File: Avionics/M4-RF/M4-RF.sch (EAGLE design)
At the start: 25 parts, among them J1 132134RP, U1 CC1120, U2 CC1190, U3 CC2520, U4 CC2592, U5 INF-PG-LQFP-100-11-7000X7000E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

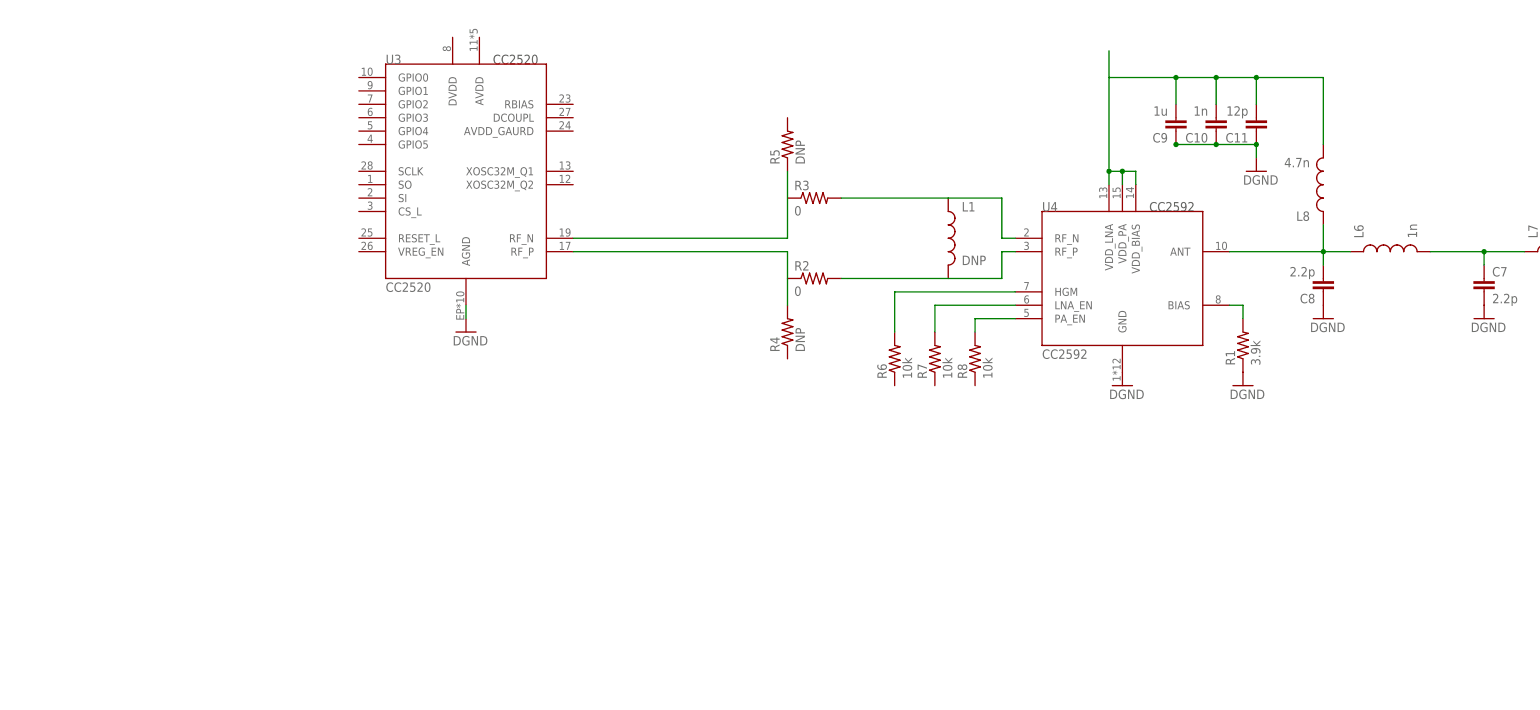
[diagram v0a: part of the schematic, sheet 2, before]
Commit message: Fixed library references and added balun to 2.4GHz circuit
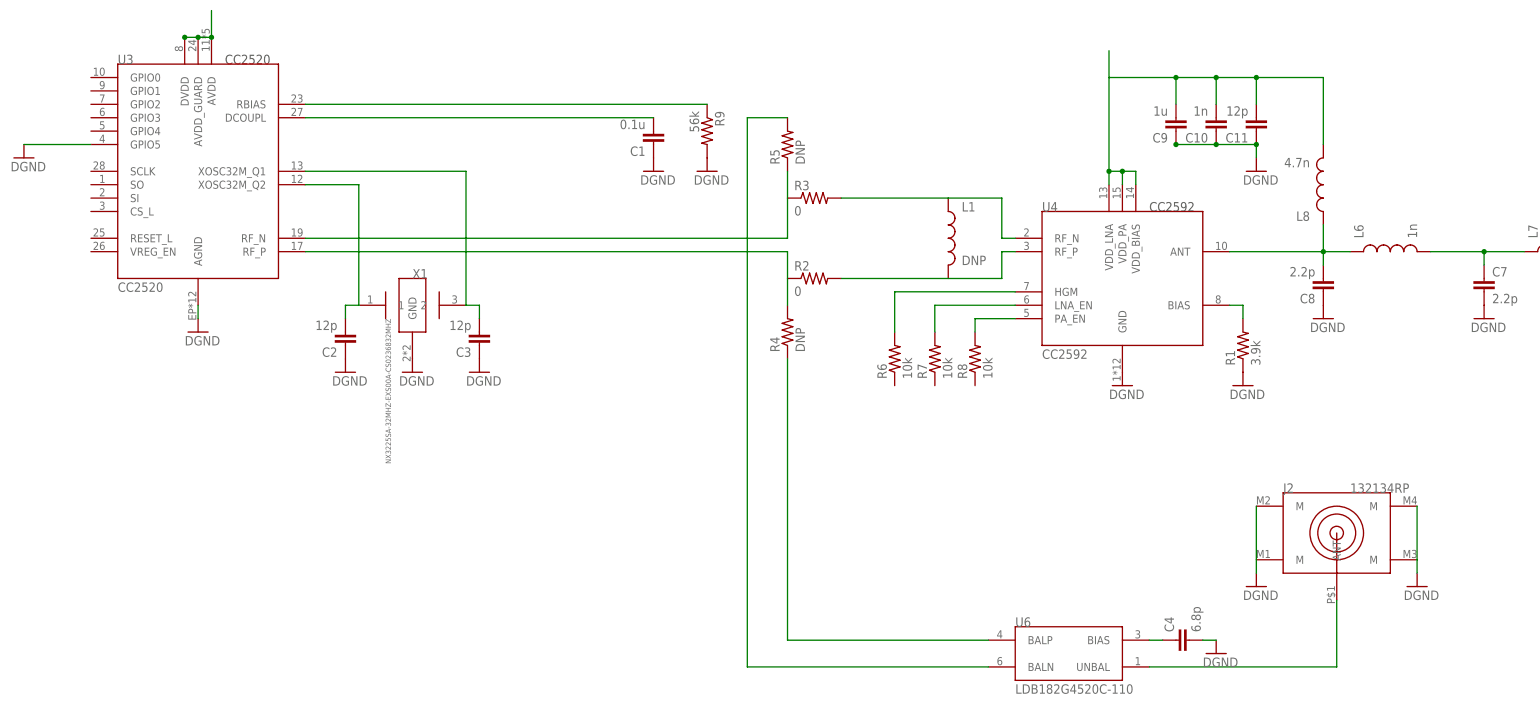
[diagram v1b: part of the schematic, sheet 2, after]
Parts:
- added C1: 0.1u, SparkFun-Capacitors:CAP0402-CAP
- added C2, C3: 12p, SparkFun-Capacitors:CAP0402-CAP
- added C4: 6.8p, SparkFun-Capacitors:CAP0402-CAP
- added J2: 132134RP, connectors:132134RP
- added R9: 56k, SparkFun-Resistors:RESISTOR0402-RES
- added U6: LDB182G4520C-110, rf:LDB182G4520C-110
- added X1: NX3225SA-32MHZ-EXS00A-CS0236832MHZ, oscillators:NX3225SA-32MHZ-EXS00A-CS0236832MHZ
- U1: device ti_rf:CC1120 -> rf:CC1120
- U2: device ti_rf:CC1190 -> rf:CC1190
- U3: device ti_rf:CC2520 -> rf:CC2520
- U4: device ti_rf:CC2592 -> rf:CC2592
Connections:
- net N$12 renamed 2G4_HG
- new net 2G4_LP: J2.ANT
- new net N$14: U3.AVDD, U3.AVDD_GUARD, U3.DVDD
- new net N$15: C2.2, U3.XOSC32M_Q2, X1.1
- new net N$16: R9.1, U3.RBIAS
- new net N$17: C1.2, U3.DCOUPL
- new net N$18: C3.2, U3.XOSC32M_Q1, X1.2
- new net N$19: R4.1, U6.BALP
- new net N$20: R5.2, U6.BALN
- new net N$21: U6.UNBAL
- new net N$22: C4.1, U6.BIAS
- net GND: now also C1.1, C2.1, C3.1, C4.2, J2.M@1, J2.M@2, J2.M@3, J2.M@4, R9.2, U3.GPIO5, X1.GND
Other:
- moved on the sheet: U3

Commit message: Applied DRU
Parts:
- removed J2: 132134RP, connectors:132134RP
- added R10: DNP, SparkFun-Resistors:RESISTOR0402-RES
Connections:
- removed net N$21: U6.UNBAL
- net 2G4_HG: now also R10.2
- net 2G4_LP: now also R10.1, U6.UNBAL; no longer J2.ANT
- net GND: now also U1.GND, U2.GND; no longer J2.M@1, J2.M@2, J2.M@3, J2.M@4
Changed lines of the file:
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@@
 <part name="C4" library="SparkFun-Capacitors" deviceset="CAP" device="0402-CAP" value="6.8p"/>
 <part name="GND16" library="SparkFun-Aesthetics" deviceset="DGND" device=""/>
-<part name="J2" library="connectors" deviceset="132134RP" device=""/>
+<part name="R10" library="SparkFun-Resistors" deviceset="RESISTOR" device="0402-RES" value="DNP"/>
 <part name="GND17" library="SparkFun-Aesthetics" deviceset="DGND" device=""/>
 <part name="GND18" library="SparkFun-Aesthetics" deviceset="DGND" device=""/>
@@
 <instance part="U1" gate="G$1" x="-38.1" y="0"/>
 <instance part="U2" gate="G$1" x="58.42" y="2.54"/>
+<instance part="GND17" gate="G$1" x="-38.1" y="-30.48"/>
+<instance part="GND18" gate="G$1" x="58.42" y="-25.4"/>
 </instances>
 <busses>
 </busses>
 <nets>
+<net name="GND" class="0">
+<segment>
+<pinref part="U1" gate="G$1" pin="GND"/>
+<pinref part="GND17" gate="G$1" pin="GND"/>
+<wire x1="-38.1" y1="-27.94" x2="-38.1" y2="-25.4" width="0.1524" layer="91"/>
+</segment>
+<segment>
+<pinref part="U2" gate="G$1" pin="GND"/>
+<pinref part="GND18" gate="G$1" pin="GND"/>
+<wire x1="58.42" y1="-22.86" x2="58.42" y2="-15.24" width="0.1524" layer="91"/>
+</segment>
+</net>
 </nets>
 </sheet>
@@
 <instance part="C4" gate="G$1" x="116.84" y="-88.9" rot="R90"/>
 <instance part="GND16" gate="G$1" x="121.92" y="-91.44"/>
-<instance part="J2" gate="G$1" x="144.78" y="-68.58"/>
-<instance part="GND17" gate="G$1" x="129.54" y="-78.74"/>
-<instance part="GND18" gate="G$1" x="160.02" y="-78.74"/>
+<instance part="R10" gate="G$1" x="241.3" y="-20.32" rot="R90"/>
 </instances>
 <busses>
@@
 <pinref part="GND16" gate="G$1" pin="GND"/>
 <wire x1="121.92" y1="-88.9" x2="119.38" y2="-88.9" width="0.1524" layer="91"/>
-</segment>
-<segment>
-<pinref part="J2" gate="G$1" pin="M@2"/>
-<pinref part="J2" gate="G$1" pin="M@1"/>
-<wire x1="129.54" y1="-63.5" x2="129.54" y2="-73.66" width="0.1524" layer="91"/>
-<wire x1="129.54" y1="-73.66" x2="129.54" y2="-76.2" width="0.1524" layer="91"/>
-<pinref part="GND17" gate="G$1" pin="GND"/>
-</segment>
-<segment>
-<pinref part="J2" gate="G$1" pin="M@4"/>
-<pinref part="J2" gate="G$1" pin="M@3"/>
-<wire x1="160.02" y1="-63.5" x2="160.02" y2="-73.66" width="0.1524" layer="91"/>
-<wire x1="160.02" y1="-73.66" x2="160.02" y2="-76.2" width="0.1524" layer="91"/>
-<pinref part="GND18" gate="G$1" pin="GND"/>
 </segment>
 </net>
@@
 <pinref part="J1" gate="G$1" pin="ANT"/>
 <wire x1="241.3" y1="-15.24" x2="241.3" y2="-2.54" width="0.1524" layer="91"/>
+<pinref part="R10" gate="G$1" pin="2"/>
+<junction x="241.3" y="-15.24"/>
 </segment>
 </net>
@@
 </segment>
 </net>
-<net name="N$21" class="0">
-<segment>
-<pinref part="U6" gate="G$1" pin="UNBAL"/>
-<wire x1="109.22" y1="-93.98" x2="144.78" y2="-93.98" width="0.1524" layer="91"/>
-</segment>
-</net>
 <net name="N$22" class="0">
 <segment>
@@
 <net name="2G4_LP" class="1">
 <segment>
-<pinref part="J2" gate="G$1" pin="ANT"/>
-<wire x1="144.78" y1="-93.98" x2="144.78" y2="-81.28" width="0.1524" layer="91"/>
-</segment>
-</net>
+<pinref part="U6" gate="G$1" pin="UNBAL"/>
+<pinref part="R10" gate="G$1" pin="1"/>
+<wire x1="109.22" y1="-93.98" x2="241.3" y2="-93.98" width="0.1524" layer="91"/>
+<wire x1="241.3" y1="-93.98" x2="241.3" y2="-25.4" width="0.1524" layer="91"/>
+</segment>
+</net>

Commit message: Added more updates to board layout.
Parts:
- removed L1: DNP, SparkFun-Passives:INDUCTOR0402
- removed R4, R5: DNP, SparkFun-Resistors:RESISTOR0402-RES
- R2: value 0 -> RESISTOR-3PIN-LH-0402; device SparkFun-Resistors:RESISTOR0402-RES -> SparkFun-Resistors:RESISTOR-3PIN-LH-0402
- R3: value 0 -> RESISTOR-3PIN-RH-0402; device SparkFun-Resistors:RESISTOR0402-RES -> SparkFun-Resistors:RESISTOR-3PIN-RH-0402
- X1: value NX3225SA-32MHZ-EXS00A-CS0236832MHZ -> FA-20H32.0000MF20X-K3; device oscillators:NX3225SA-32MHZ-EXS00A-CS0236832MHZ -> oscillators:FA-20H32.0000MF20X-K3
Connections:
- removed net N$4: L1.1, R3.2, U4.RF_N
- new net N$12: R3.1, U4.RF_N
- net N$1: now also R3.2; no longer R3.1, R5.1
- net N$19: now also R2.3; no longer R4.1
- net N$2: now also R2.2; no longer R2.1, R4.2
- net N$20: now also R3.3; no longer R5.2
- net N$6: now also R2.1; no longer L1.2, R2.2
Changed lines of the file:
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@@
 <part name="U4" library="rf" deviceset="CC2592" device=""/>
 <part name="U5" library="XMC4500-F100K1024 AB" deviceset="INF-PG-LQFP-100-11-7000X7000E9" device="LQFP-100"/>
-<part name="L1" library="SparkFun-Passives" deviceset="INDUCTOR" device="0402" value="DNP"/>
 <part name="L6" library="SparkFun-Passives" deviceset="INDUCTOR" device="0402" value="1n"/>
 <part name="L7" library="SparkFun-Passives" deviceset="INDUCTOR" device="0402" value="2n"/>
@@
 <part name="GND5" library="SparkFun-Aesthetics" deviceset="DGND" device=""/>
 <part name="GND7" library="SparkFun-Aesthetics" deviceset="DGND" device=""/>
-<part name="R3" library="SparkFun-Resistors" deviceset="RESISTOR" device="0402-RES" value="0"/>
-<part name="R2" library="SparkFun-Resistors" deviceset="RESISTOR" device="0402-RES" value="0"/>
-<part name="R4" library="SparkFun-Resistors" deviceset="RESISTOR" device="0402-RES" value="DNP"/>
-<part name="R5" library="SparkFun-Resistors" deviceset="RESISTOR" device="0402-RES" value="DNP"/>
 <part name="GND1" library="SparkFun-Aesthetics" deviceset="DGND" device=""/>
 <part name="R6" library="SparkFun-Resistors" deviceset="RESISTOR" device="0402-RES" value="10k"/>
@@
 <part name="C1" library="SparkFun-Capacitors" deviceset="CAP" device="0402-CAP" value="0.1u"/>
 <part name="GND11" library="SparkFun-Aesthetics" deviceset="DGND" device=""/>
-<part name="X1" library="oscillators" deviceset="NX3225SA-32MHZ-EXS00A-CS02368" device="32MHZ"/>
+<part name="X1" library="oscillators" deviceset="FA-20H" device="32.0000MF20X-K3"/>
 <part name="GND12" library="SparkFun-Aesthetics" deviceset="DGND" device=""/>
 <part name="C2" library="SparkFun-Capacitors" deviceset="CAP" device="0402-CAP" value="12p"/>
@@
 <part name="GND17" library="SparkFun-Aesthetics" deviceset="DGND" device=""/>
 <part name="GND18" library="SparkFun-Aesthetics" deviceset="DGND" device=""/>
+<part name="R2" library="SparkFun-Resistors" deviceset="RESISTOR-3PIN-LH" device="-0402"/>
+<part name="R3" library="SparkFun-Resistors" deviceset="RESISTOR-3PIN-RH" device="-0402"/>
 </parts>
 <sheets>
@@
 <instance part="U3" gate="G$1" x="-71.12" y="0"/>
 <instance part="U4" gate="G$1" x="104.14" y="-22.86"/>
-<instance part="L1" gate="G$1" x="71.12" y="-12.7"/>
 <instance part="L6" gate="G$1" x="154.94" y="-15.24" rot="R90"/>
 <instance part="L7" gate="G$1" x="187.96" y="-15.24" rot="R90"/>
@@
 <instance part="GND5" gate="G$1" x="127" y="-40.64"/>
 <instance part="GND7" gate="G$1" x="129.54" y="0"/>
-<instance part="R3" gate="G$1" x="45.72" y="-5.08"/>
-<instance part="R2" gate="G$1" x="45.72" y="-20.32"/>
-<instance part="R4" gate="G$1" x="40.64" y="-30.48" rot="R90"/>
-<instance part="R5" gate="G$1" x="40.64" y="5.08" rot="R90"/>
 <instance part="GND1" gate="G$1" x="104.14" y="-40.64"/>
 <instance part="R6" gate="G$1" x="60.96" y="-35.56" rot="R90"/>
@@
 <instance part="GND16" gate="G$1" x="121.92" y="-91.44"/>
 <instance part="R10" gate="G$1" x="241.3" y="-20.32" rot="R90"/>
+<instance part="R2" gate="G$1" x="48.26" y="-15.24" smashed="yes" rot="R180">
+<attribute name="NAME" x="46.99" y="-18.8214" size="1.778" layer="95"/>
+<attribute name="VALUE" x="46.99" y="-21.082" size="1.778" layer="96"/>
+</instance>
+<instance part="R3" gate="G$1" x="48.26" y="-12.7" smashed="yes" rot="R180">
+<attribute name="NAME" x="46.99" y="-11.2014" size="1.778" layer="95"/>
+<attribute name="VALUE" x="46.99" y="-8.382" size="1.778" layer="96"/>
+</instance>
 </instances>
 <busses>
@@
 <pinref part="U3" gate="G$1" pin="RF_N"/>
 <wire x1="-50.8" y1="-12.7" x2="40.64" y2="-12.7" width="0.1524" layer="91"/>
-<pinref part="R3" gate="G$1" pin="1"/>
-<wire x1="40.64" y1="-12.7" x2="40.64" y2="-5.08" width="0.1524" layer="91"/>
-<pinref part="R5" gate="G$1" pin="1"/>
-<wire x1="40.64" y1="-5.08" x2="40.64" y2="0" width="0.1524" layer="91"/>
+<pinref part="R3" gate="G$1" pin="2"/>
 </segment>
 </net>
@@
 <pinref part="U3" gate="G$1" pin="RF_P"/>
 <wire x1="-50.8" y1="-15.24" x2="40.64" y2="-15.24" width="0.1524" layer="91"/>
+<pinref part="R2" gate="G$1" pin="2"/>
+</segment>
+</net>
+<net name="N$6" class="0">
+<segment>
+<pinref part="U4" gate="G$1" pin="RF_P"/>
 <pinref part="R2" gate="G$1" pin="1"/>
-<wire x1="40.64" y1="-20.32" x2="40.64" y2="-15.24" width="0.1524" layer="91"/>
-<pinref part="R4" gate="G$1" pin="2"/>
-<wire x1="40.64" y1="-20.32" x2="40.64" y2="-25.4" width="0.1524" layer="91"/>
-</segment>
-</net>
-<net name="N$4" class="0">
-<segment>
-<pinref part="L1" gate="G$1" pin="1"/>
-<wire x1="71.12" y1="-5.08" x2="81.28" y2="-5.08" width="0.1524" layer="91"/>
-<wire x1="81.28" y1="-5.08" x2="81.28" y2="-12.7" width="0.1524" layer="91"/>
-<pinref part="U4" gate="G$1" pin="RF_N"/>
-<wire x1="81.28" y1="-12.7" x2="83.82" y2="-12.7" width="0.1524" layer="91"/>
-<pinref part="R3" gate="G$1" pin="2"/>
-<wire x1="50.8" y1="-5.08" x2="71.12" y2="-5.08" width="0.1524" layer="91"/>
-</segment>
-</net>
-<net name="N$6" class="0">
-<segment>
-<pinref part="L1" gate="G$1" pin="2"/>
-<wire x1="71.12" y1="-20.32" x2="81.28" y2="-20.32" width="0.1524" layer="91"/>
-<wire x1="81.28" y1="-20.32" x2="81.28" y2="-15.24" width="0.1524" layer="91"/>
-<pinref part="U4" gate="G$1" pin="RF_P"/>
-<wire x1="81.28" y1="-15.24" x2="83.82" y2="-15.24" width="0.1524" layer="91"/>
-<pinref part="R2" gate="G$1" pin="2"/>
-<wire x1="71.12" y1="-20.32" x2="50.8" y2="-20.32" width="0.1524" layer="91"/>
+<wire x1="53.34" y1="-15.24" x2="83.82" y2="-15.24" width="0.1524" layer="91"/>
 </segment>
 </net>
@@
 <net name="N$19" class="0">
 <segment>
-<pinref part="R4" gate="G$1" pin="1"/>
-<wire x1="40.64" y1="-35.56" x2="40.64" y2="-88.9" width="0.1524" layer="91"/>
+<wire x1="43.18" y1="-25.4" x2="43.18" y2="-88.9" width="0.1524" layer="91"/>
 <pinref part="U6" gate="G$1" pin="BALP"/>
-<wire x1="40.64" y1="-88.9" x2="78.74" y2="-88.9" width="0.1524" layer="91"/>
+<wire x1="43.18" y1="-88.9" x2="78.74" y2="-88.9" width="0.1524" layer="91"/>
+<pinref part="R2" gate="G$1" pin="3"/>
 </segment>
 </net>
@@
 <pinref part="U6" gate="G$1" pin="BALN"/>
 <wire x1="78.74" y1="-93.98" x2="33.02" y2="-93.98" width="0.1524" layer="91"/>
-<wire x1="33.02" y1="-93.98" x2="33.02" y2="10.16" width="0.1524" layer="91"/>
-<pinref part="R5" gate="G$1" pin="2"/>
-<wire x1="33.02" y1="10.16" x2="40.64" y2="10.16" width="0.1524" layer="91"/>
+<wire x1="33.02" y1="-93.98" x2="33.02" y2="-2.54" width="0.1524" layer="91"/>
+<wire x1="33.02" y1="-2.54" x2="43.18" y2="-2.54" width="0.1524" layer="91"/>
+<pinref part="R3" gate="G$1" pin="3"/>
 </segment>
 </net>
@@
 </segment>
 </net>
+<net name="N$12" class="0">
+<segment>
+<pinref part="U4" gate="G$1" pin="RF_N"/>
+<pinref part="R3" gate="G$1" pin="1"/>
+<wire x1="83.82" y1="-12.7" x2="53.34" y2="-12.7" width="0.1524" layer="91"/>
+</segment>
+</net>

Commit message: Finished first draft of 2.4GHz layout.
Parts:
- removed R10: DNP, SparkFun-Resistors:RESISTOR0402-RES
- added J2: 132134RP, connectors:132134RP
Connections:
- removed net 2G4_HG: C6.2, J1.ANT, R10.2
- new net 2G4_LG: C6.2, J1.ANT
- net 2G4_LP: now also J2.ANT; no longer R10.1
- net GND: now also J2.M@1, J2.M@2, J2.M@3, J2.M@4
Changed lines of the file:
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@@
 <class number="0" name="default" width="0" drill="0">
 </class>
-<class number="1" name="50 ohm" width="0.2032" drill="0">
+<class number="1" name="50 ohm" width="0.3048" drill="0">
 </class>
 </classes>
@@
 <part name="C4" library="SparkFun-Capacitors" deviceset="CAP" device="0402-CAP" value="6.8p"/>
 <part name="GND16" library="SparkFun-Aesthetics" deviceset="DGND" device=""/>
-<part name="R10" library="SparkFun-Resistors" deviceset="RESISTOR" device="0402-RES" value="DNP"/>
 <part name="GND17" library="SparkFun-Aesthetics" deviceset="DGND" device=""/>
 <part name="GND18" library="SparkFun-Aesthetics" deviceset="DGND" device=""/>
 <part name="R2" library="SparkFun-Resistors" deviceset="RESISTOR-3PIN-LH" device="-0402"/>
 <part name="R3" library="SparkFun-Resistors" deviceset="RESISTOR-3PIN-RH" device="-0402"/>
+<part name="J2" library="connectors" deviceset="132134RP" device=""/>
+<part name="GND19" library="SparkFun-Aesthetics" deviceset="DGND" device=""/>
+<part name="GND20" library="SparkFun-Aesthetics" deviceset="DGND" device=""/>
 </parts>
 <sheets>
@@
 <instance part="C4" gate="G$1" x="116.84" y="-88.9" rot="R90"/>
 <instance part="GND16" gate="G$1" x="121.92" y="-91.44"/>
-<instance part="R10" gate="G$1" x="241.3" y="-20.32" rot="R90"/>
 <instance part="R2" gate="G$1" x="48.26" y="-15.24" smashed="yes" rot="R180">
 <attribute name="NAME" x="46.99" y="-18.8214" size="1.778" layer="95"/>
@@
 <attribute name="VALUE" x="46.99" y="-8.382" size="1.778" layer="96"/>
 </instance>
+<instance part="J2" gate="G$1" x="152.4" y="-66.04"/>
+<instance part="GND19" gate="G$1" x="137.16" y="-76.2"/>
+<instance part="GND20" gate="G$1" x="167.64" y="-76.2"/>
 </instances>
 <busses>
 </busses>
 <nets>
-<net name="N$1" class="0">
+<net name="N$1" class="1">
 <segment>
 <pinref part="U3" gate="G$1" pin="RF_N"/>
@@
 </segment>
 </net>
-<net name="N$2" class="0">
+<net name="N$2" class="1">
 <segment>
 <pinref part="U3" gate="G$1" pin="RF_P"/>
@@
 </segment>
 </net>
-<net name="N$6" class="0">
+<net name="N$6" class="1">
 <segment>
 <pinref part="U4" gate="G$1" pin="RF_P"/>
@@
 <wire x1="121.92" y1="-88.9" x2="119.38" y2="-88.9" width="0.1524" layer="91"/>
 </segment>
-</net>
-<net name="N$7" class="0">
+<segment>
+<pinref part="J2" gate="G$1" pin="M@2"/>
+<pinref part="J2" gate="G$1" pin="M@1"/>
+<wire x1="137.16" y1="-60.96" x2="137.16" y2="-71.12" width="0.1524" layer="91"/>
+<wire x1="137.16" y1="-71.12" x2="137.16" y2="-73.66" width="0.1524" layer="91"/>
+<pinref part="GND19" gate="G$1" pin="GND"/>
+</segment>
+<segment>
+<pinref part="J2" gate="G$1" pin="M@4"/>
+<pinref part="J2" gate="G$1" pin="M@3"/>
+<wire x1="167.64" y1="-60.96" x2="167.64" y2="-71.12" width="0.1524" layer="91"/>
+<wire x1="167.64" y1="-71.12" x2="167.64" y2="-73.66" width="0.1524" layer="91"/>
+<pinref part="GND20" gate="G$1" pin="GND"/>
+</segment>
+</net>
+<net name="N$7" class="1">
 <segment>
 <pinref part="U4" gate="G$1" pin="ANT"/>
@@
 </segment>
 </net>
-<net name="N$8" class="0">
+<net name="N$8" class="1">
 <segment>
 <pinref part="C7" gate="G$1" pin="1"/>
@@
 </segment>
 </net>
-<net name="N$9" class="0">
+<net name="N$9" class="1">
 <segment>
 <pinref part="L7" gate="G$1" pin="2"/>
@@
 </segment>
 </net>
-<net name="2G4_HG" class="1">
+<net name="2G4_LG" class="1">
 <segment>
 <pinref part="C6" gate="G$1" pin="2"/>
@@
 <pinref part="J1" gate="G$1" pin="ANT"/>
 <wire x1="241.3" y1="-15.24" x2="241.3" y2="-2.54" width="0.1524" layer="91"/>
-<pinref part="R10" gate="G$1" pin="2"/>
-<junction x="241.3" y="-15.24"/>
 </segment>
 </net>
@@
 </segment>
 </net>
-<net name="N$19" class="0">
+<net name="N$19" class="1">
 <segment>
 <wire x1="43.18" y1="-25.4" x2="43.18" y2="-88.9" width="0.1524" layer="91"/>
@@
 </segment>
 </net>
-<net name="N$20" class="0">
+<net name="N$20" class="1">
 <segment>
 <pinref part="U6" gate="G$1" pin="BALN"/>
@@
 <segment>
 <pinref part="U6" gate="G$1" pin="UNBAL"/>
-<pinref part="R10" gate="G$1" pin="1"/>
-<wire x1="109.22" y1="-93.98" x2="241.3" y2="-93.98" width="0.1524" layer="91"/>
-<wire x1="241.3" y1="-93.98" x2="241.3" y2="-25.4" width="0.1524" layer="91"/>
-</segment>
-</net>
-<net name="N$12" class="0">
+<wire x1="109.22" y1="-93.98" x2="152.4" y2="-93.98" width="0.1524" layer="91"/>
+<pinref part="J2" gate="G$1" pin="ANT"/>
+<wire x1="152.4" y1="-93.98" x2="152.4" y2="-78.74" width="0.1524" layer="91"/>
+</segment>
+</net>
+<net name="N$12" class="1">
 <segment>
 <pinref part="U4" gate="G$1" pin="RF_N"/>
